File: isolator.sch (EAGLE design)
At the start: 29 parts, among them IC1 TL494BD, Q1 BC817-16LT1SMD, Q2 BC807-16LT1SMD, Q3 BC807-16LT1SMD, Q4 BC817-16LT1SMD

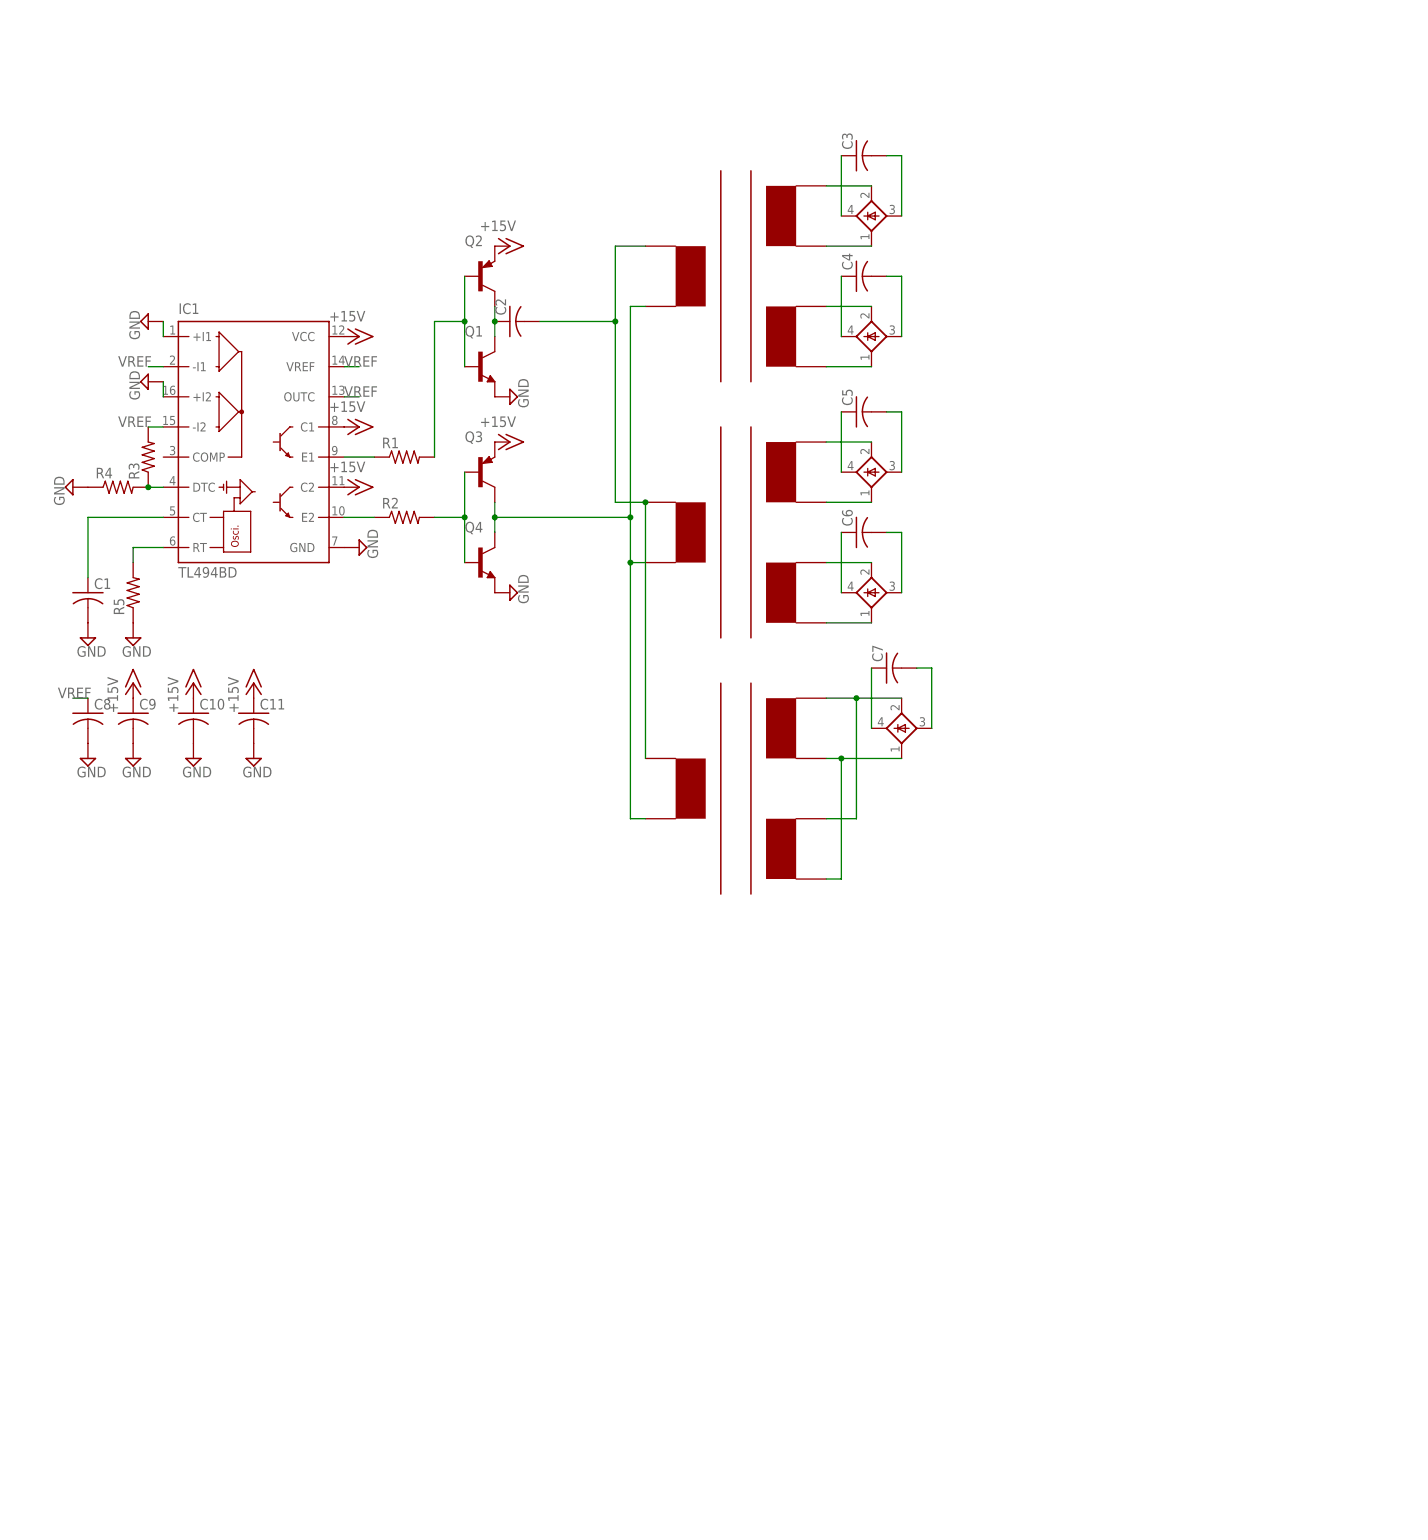
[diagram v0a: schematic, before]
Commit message: new isolator design
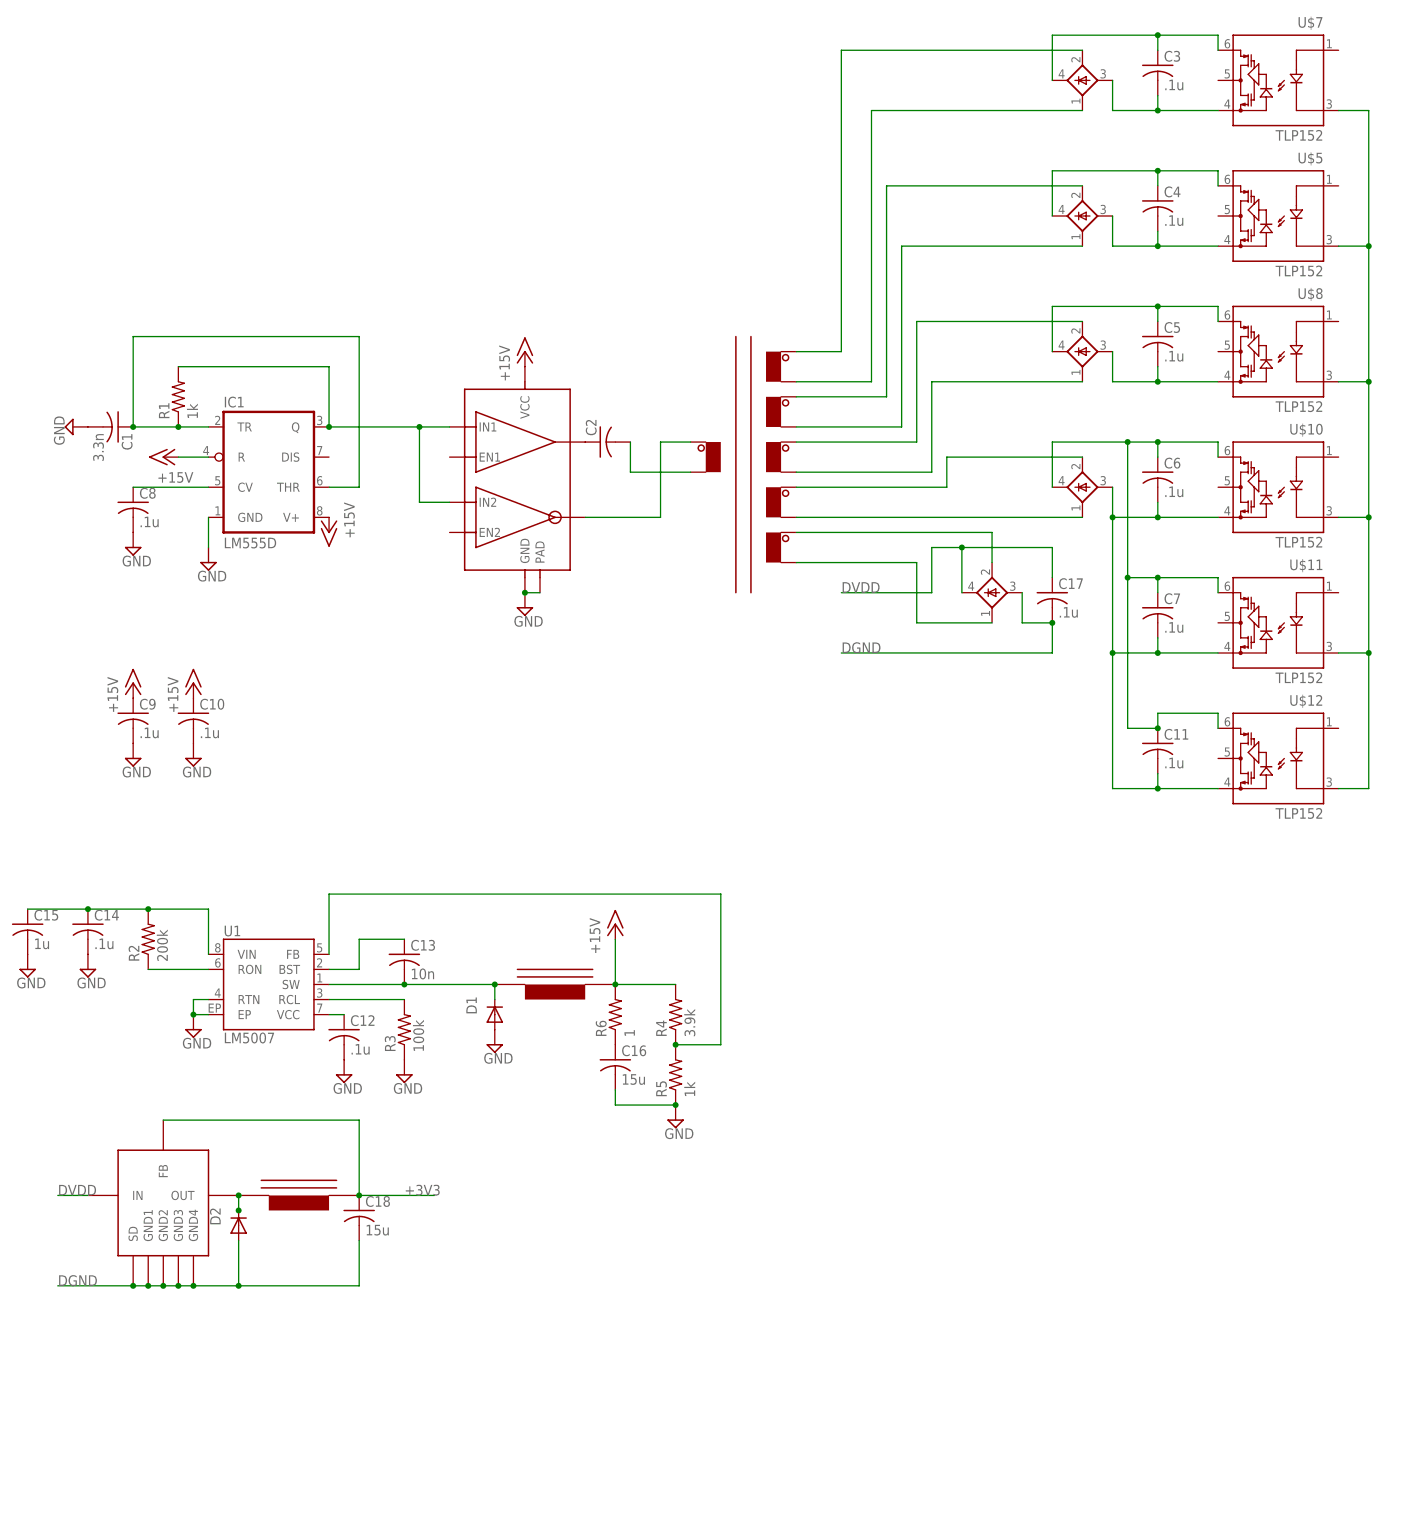
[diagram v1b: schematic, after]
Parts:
- removed Q1, Q4: BC817-16LT1SMD, transistor-npn:BC817-16LT1SMD
- removed Q2, Q3: BC807-16LT1SMD, transistor-pnp:BC807-16LT1SMD
- added C12, C14, C17: .1u, rcl:C-USC0805K
- added C13: 10n, rcl:C-USC0805K
- added C15: 1u, rcl:C-USC0805K
- added C16, C18: 15u, rcl:C-USC0805K
- added D1, D2: B170-13-F, diode:DIODE-DO214AC
- added R6: 1, resistor:R-US_M0805
- added U$10, U$11, U$12: TLP152, brushlessrage:TLP152
- added U$13, U$16: SRN6045-101M, brushlessrage:SRN6045-101M
- added U$14, U$9: BAS4002A, utesla:BAS4002A
- added U$15: AP1509, brushlessrage:AP1509
- added U1: LM5007, SparkFun-PowerIC:LM5007
- C1: value (none) -> 3.3n
- C10, C11, C3, C4, C5, C6, C7, C8, C9: value (none) -> .1u
- IC1: value TL494BD -> LM555D; device linear:TL494BD -> linear:LM555D
- R1, R5: value (none) -> 1k; device rcl:R-US_M0805 -> resistor:R-US_M0805
- R2: value (none) -> 200k; device rcl:R-US_M0805 -> resistor:R-US_M0805
- R3: value (none) -> 100k; device rcl:R-US_M0805 -> resistor:R-US_M0805
- R4: value (none) -> 3.9k; device rcl:R-US_M0805 -> resistor:R-US_M0805
- U$1: value PA0173 -> HP1; device utesla:PA0173 -> brushlessrage:HP1
- U$2: value PA0173 -> UCC27525DGN; device utesla:PA0173 -> brushlessrage:UCC27525DGN
- U$5, U$8: value BAS4002A -> TLP152; device utesla:BAS4002A -> brushlessrage:TLP152
- U$7: value PA0173 -> TLP152; device utesla:PA0173 -> brushlessrage:TLP152
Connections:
- removed net N$9: C1.1, IC1.CT
- removed net VREF: C8.1, IC1.-I1, IC1.-I2, IC1.OUTC, IC1.VREF, R3.2
- new net +3V3: C18.1, U$15.FB, U$16.P$2
- new net DGND: C17.2, C18.2, D2.A, U$10.LED-, U$11.LED-, U$12.LED-, U$14.-, U$15.GND1, U$15.GND2, U$15.GND3, U$15.GND4, U$15.SD, U$5.LED-, U$7.LED-, U$8.LED-
- new net DVDD: C17.1, U$14.+, U$15.IN
- new net N$31: C12.1, U1.VCC
- new net N$32: C13.2, D1.C, U$13.P$1, U1.SW
- new net N$33: C13.1, U1.BST
- new net N$34: R3.2, U1.RCL
- net +15V: now also IC1.R, IC1.V+, R4.2, R6.2, U$13.P$2, U$2.VCC; no longer C11.1, IC1.C1, IC1.C2, IC1.VCC, Q2.E, Q3.E
- net GND: now also C12.2, C14.2, C15.2, C16.2, D1.A, R3.1, U$2.GND, U$2.PAD, U1.EP, U1.RTN; no longer C11.2, IC1.+I1, IC1.+I2, Q1.E, Q4.E, R4.1
- net N$1: now also U$1.3B, U$3.AC1; no longer C2.2, U$1.PRIA, U$2.PRIA, U$7.PRIA
- net N$10: now also IC1.Q, R1.2, U$2.IN1, U$2.IN2; no longer C2.1, Q1.C, Q2.C
- net N$11: now also U$1.3A; no longer U$1.SEC1A
- net N$12: now also U$1.4B, U$4.AC1; no longer U$1.SEC1B, U$3.AC1
- net N$13: now also C4.1, U$4.+, U$5.VDD; no longer U$1.SEC2A, U$4.AC2
- net N$14: now also C4.2, U$4.-, U$5.GND; no longer U$1.SEC2B, U$4.AC1
- net N$15: now also U$1.5A, U$6.AC2; no longer U$2.SEC1A, U$5.AC2
- net N$16: now also U$1.5B, U$6.AC1; no longer U$2.SEC1B, U$5.AC1
- net N$17: now also C5.1, U$6.+, U$8.VDD; no longer U$2.SEC2A, U$6.AC2
- net N$18: now also C5.2, U$6.-, U$8.GND; no longer U$2.SEC2B, U$6.AC1
- net N$19: now also U$1.6A, U$9.AC2; no longer C3.1, U$3.+
- net N$2: now also C3.1, U$3.+, U$7.VDD; no longer Q3.C, Q4.C, U$1.PRIB, U$2.PRIB, U$7.PRIB
- net N$20: now also U$1.6B, U$9.AC1; no longer C3.2, U$3.-
- net N$21: now also C14.1, C15.1, R2.2, U1.VIN; no longer C4.1, U$4.+
- net N$22: now also C11.2, C6.2, C7.2, U$10.GND, U$11.GND, U$12.GND, U$9.-; no longer C4.2, U$4.-
- net N$23: now also C16.1, R6.1; no longer C5.1, U$5.+
- net N$24: now also U$1.2A, U$14.AC2; no longer C5.2, U$5.-
- net N$25: now also C11.1, C7.1, U$10.VDD, U$11.VDD, U$12.VDD, U$9.+; no longer U$6.+
- net N$26: now also R4.1, R5.2, U1.FB; no longer C6.2, U$6.-
- net N$27: now also U$1.2B, U$14.AC1; no longer U$7.SEC1A, U$7.SEC2A, U$8.AC2
- net N$28: now also R2.1, U1.RON; no longer U$7.SEC1B, U$7.SEC2B, U$8.AC1
- net N$29: now also D2.C, U$15.OUT, U$16.P$1; no longer C7.1, U$8.+
- net N$3: now also C3.2, U$3.-, U$7.GND; no longer Q1.B, Q2.B, R1.2
- net N$30: now also C2.2, U$1.1B; no longer C7.2, U$8.-
- net N$4: now also C2.1, U$2.OUT1; no longer Q3.B, Q4.B, R2.2
- net N$5: now also U$1.1A, U$2.OUT2; no longer IC1.E1, R1.1
- net N$6: now also C1.1, IC1.THR, IC1.TR, R1.1; no longer IC1.E2, R2.1
- net N$7: now also U$1.4A, U$4.AC2; no longer IC1.DTC, R3.1, R4.2
- net N$8: now also C8.1, IC1.CV; no longer IC1.RT, R5.2
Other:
- moved on the sheet: C1, C11, C2, C3, C4, C5, C6, C7, C8, R1, R2, R3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

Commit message: up-to-date brushlessrage.lbr, updated isolator for send-out
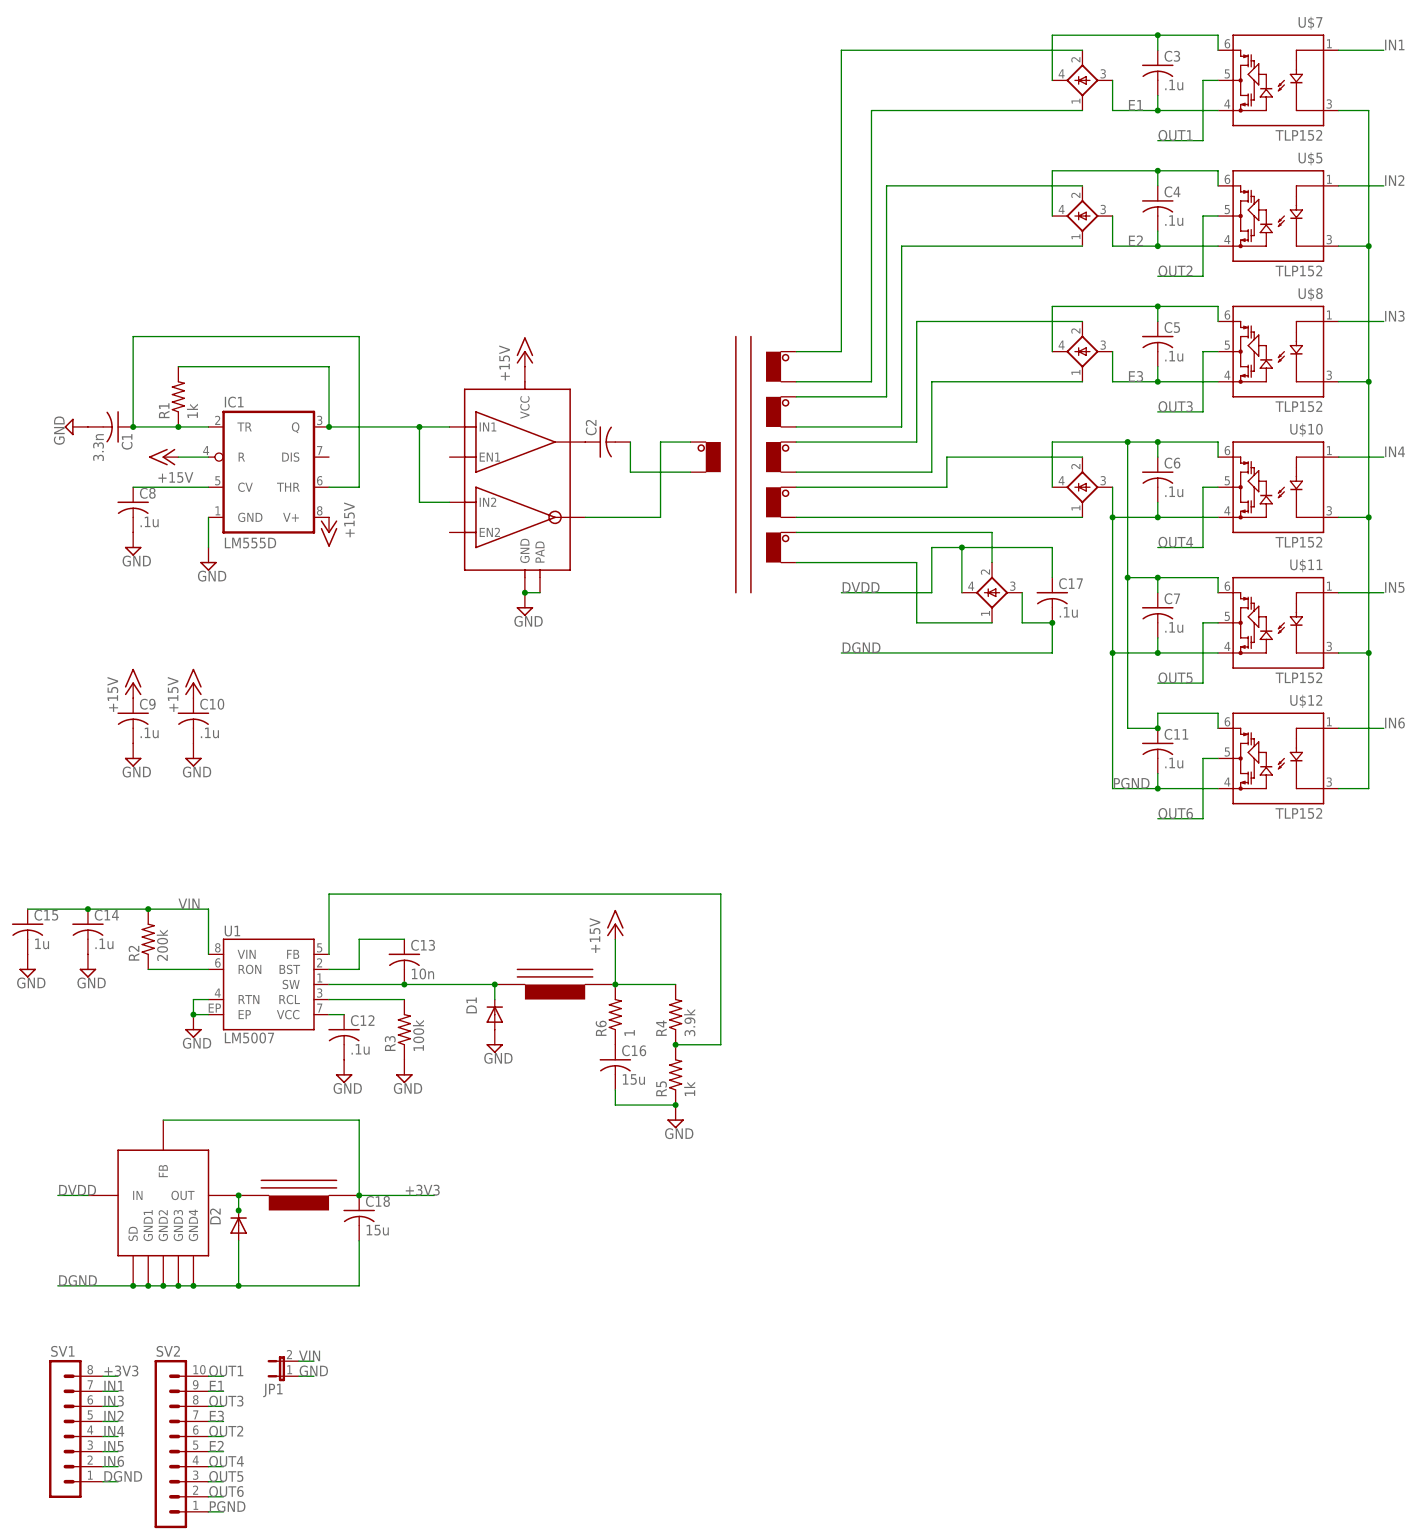
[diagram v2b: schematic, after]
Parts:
- added JP1: (no value), jumper:JP1E
- added SV1: (no value), con-lstb:MA08-1
- added SV2: (no value), con-lstb:MA10-1
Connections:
- removed net N$14: C4.2, U$4.-, U$5.GND
- removed net N$18: C5.2, U$6.-, U$8.GND
- removed net N$21: C14.1, C15.1, R2.2, U1.VIN
- removed net N$22: C11.2, C6.2, C7.2, U$10.GND, U$11.GND, U$12.GND, U$9.-
- removed net N$3: C3.2, U$3.-, U$7.GND
- new net E1: C3.2, SV2.9, U$3.-, U$7.GND
- new net E2: C4.2, SV2.5, U$4.-, U$5.GND
- new net E3: C5.2, SV2.7, U$6.-, U$8.GND
- new net IN1: SV1.7, U$7.LED+
- new net IN2: SV1.5, U$5.LED+
- new net IN3: SV1.6, U$8.LED+
- new net IN4: SV1.4, U$10.LED+
- new net IN5: SV1.3, U$11.LED+
- new net IN6: SV1.2, U$12.LED+
- new net OUT1: SV2.10, U$7.VO
- new net OUT2: SV2.6, U$5.VO
- new net OUT3: SV2.8, U$8.VO
- new net OUT4: SV2.4, U$10.VO
- new net OUT5: SV2.3, U$11.VO
- new net OUT6: SV2.2, U$12.VO
- new net PGND: C11.2, C6.2, C7.2, SV2.1, U$10.GND, U$11.GND, U$12.GND, U$9.-
- new net VIN: C14.1, C15.1, JP1.2, R2.2, U1.VIN
- net +3V3: now also SV1.8
- net DGND: now also SV1.1
- net GND: now also JP1.1
